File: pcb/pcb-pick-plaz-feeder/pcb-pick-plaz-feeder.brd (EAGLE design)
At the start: 70 x 50 mm, 59 parts, among them T1 MMBT2222, U1 LDO-1117, U2 STM32F030CCT6, U3 DRV8833PWPR, X1 PIN_1X1SMD_BIG_L, X2 PIN_1X1SMD_BIG_L, X3 PIN_1X1SMD_BIG_L, X4 PIN_1X1SMD_BIG_L, X5 PIN_5X1HD, X6 PIN_1X1SMD_BIG_L, X7 PIN_1X1SMD_BIG_L

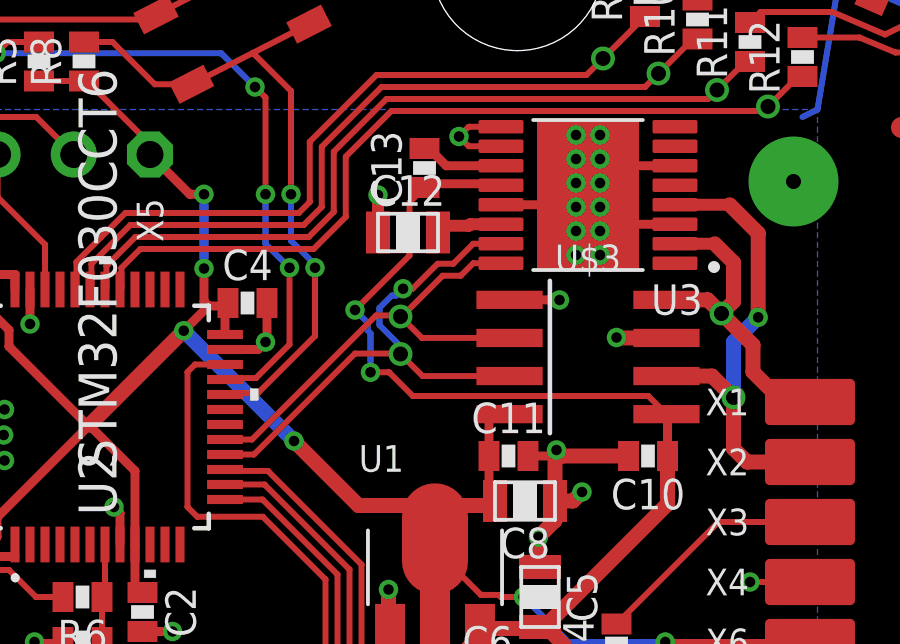
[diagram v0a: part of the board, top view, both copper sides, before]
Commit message: updated pcbs with step files
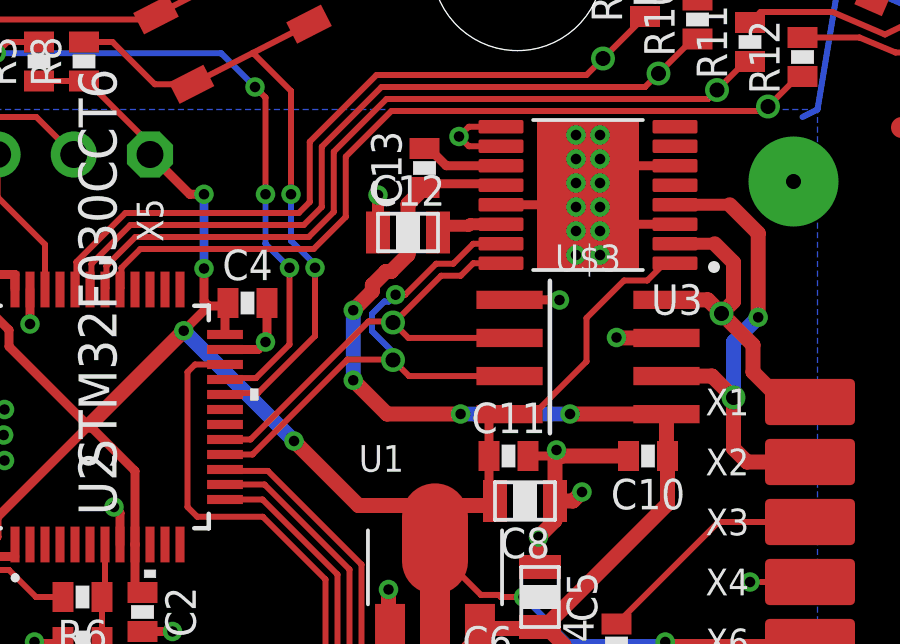
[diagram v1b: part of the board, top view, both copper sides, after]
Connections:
- net +3V3: now also U3.1
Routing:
- net +3V3: track 95.1 -> 103.6 mm
- net +5V: track 55.5 -> 56.1 mm, vias 2 -> 4
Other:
- board text added: "pcb-pick-plaz-feeder v1b by ftobler 2022"
- board text removed: "pcb-pick-plaz-feeder v1 by ftobler 2022"
